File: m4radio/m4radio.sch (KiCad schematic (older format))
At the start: 36 parts, among them IC1 MCP2562, IC2 STM32F405RxTx, J1 WEST TOP, J2 EAST TOP, P1 SWD_TC, Y1 26M

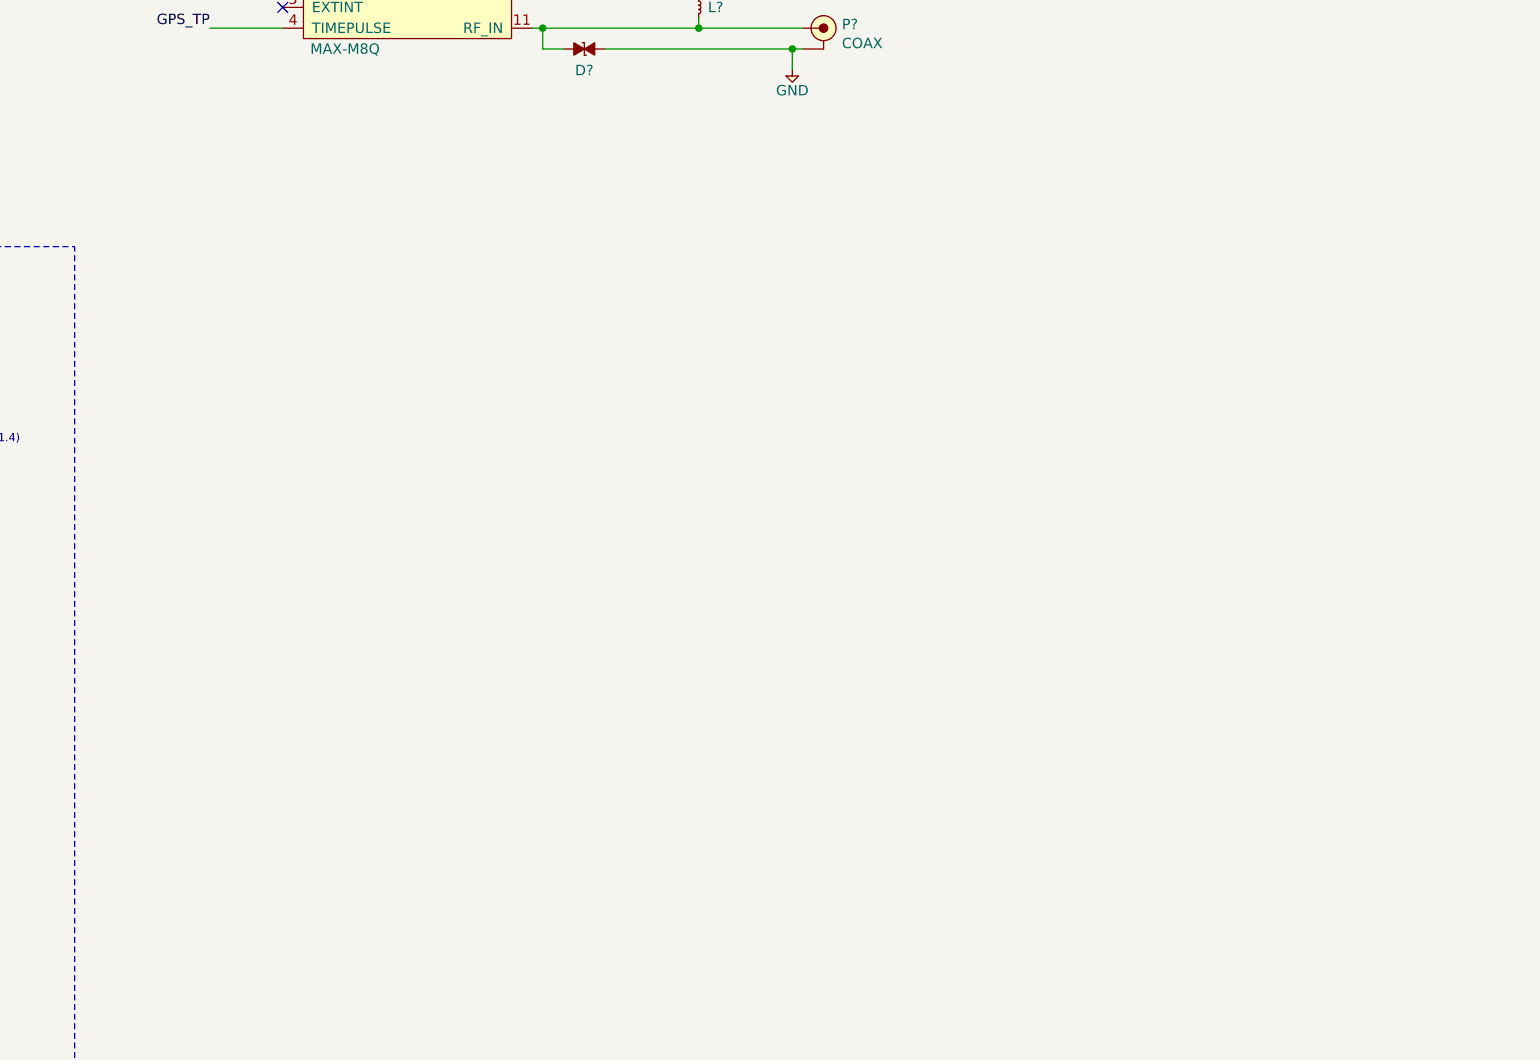
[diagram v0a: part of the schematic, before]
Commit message: Add PLL and radio ICs to schematic
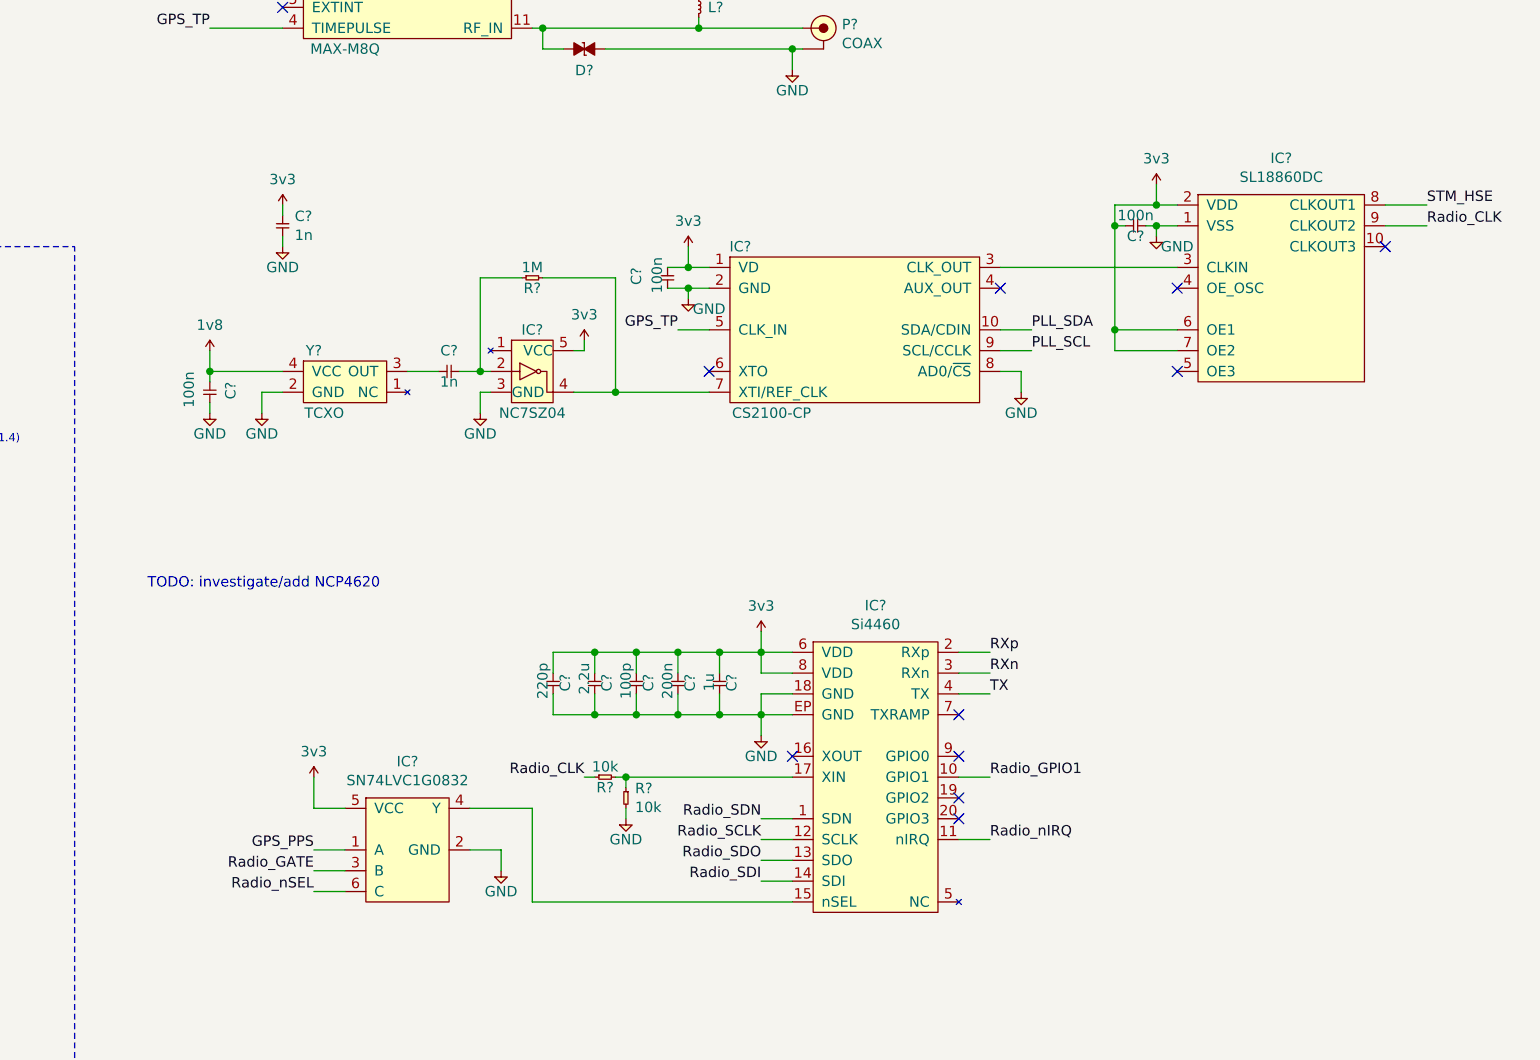
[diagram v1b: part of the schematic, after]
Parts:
- added C? (x3): 100n, symbol agg-kicad:C
- added C? (x2): 1n, symbol agg-kicad:C
- added C?: 1u, symbol agg-kicad:C
- added C?: 200n, symbol agg-kicad:C
- added C?: 100p, symbol agg-kicad:C
- added C?: 2.2u, symbol agg-kicad:C
- added C?: 220p, symbol agg-kicad:C
- added IC?: NC7SZ04, agg:SOT-23-5, symbol agg-kicad:NC7SZ04
- added IC?: CS2100-CP, agg:MSOP-10, symbol agg-kicad:CS2100-CP
- added IC?: SL18860DC, agg:DFN-10-SL18860DC, symbol agg-kicad:SL18860DC
- added IC?: SN74LVC1G0832, agg:SC-70-6, symbol agg-kicad:SN74LVC1G0832
- added IC?: Si4460, agg:QFN-20-EP-SI, symbol agg-kicad:Si4460
- added R?: 1M, symbol agg-kicad:R
- added R? (x2): 10k, symbol agg-kicad:R
- added Y?: TCXO, symbol agg-kicad:TCXO
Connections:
- net 3v3: now also C?.1, C?.1, C?.1, C?.1, C?.1, C?.1, C?.1, C?.2, IC?.1 (VD), IC?.2 (VDD), IC?.5 (VCC), IC?.5 (VCC), IC?.6 (OE1), IC?.6 (VDD), IC?.7 (OE2), IC?.8 (VDD)
- net GND: now also C?.1, C?.2, C?.2, C?.2, C?.2, C?.2, C?.2, C?.2, C?.2, IC?.1 (VSS), IC?.18 (GND), IC?.2 (GND), IC?.2 (GND), IC?.3 (GND), IC?.8 (AD0/~CS), IC?.EP (GND), R?.2, Y?.2 (GND)
- net GPS_PPS: now also IC?.1 (A)
- net GPS_TP: now also IC?.5 (CLK_IN)
- new net: C?.1, Y?.3 (OUT)
- new net: C?.2, IC?.2, R?.1
- new net: IC?.4, IC?.7 (XTI/REF_CLK), R?.2
- new net: IC?.3 (CLKIN), IC?.3 (CLK_OUT)
- new net: IC?.15 (nSEL), IC?.4 (Y)
- new net: IC?.17 (XIN), R?.1, R?.2
- new net 1v8: C?.1, Y?.4 (VCC)
- new net PLL_SCL: IC?.9 (SCL/CCLK)
- new net PLL_SDA: IC?.10 (SDA/CDIN)
- new net RXn: IC?.3 (RXn)
- new net RXp: IC?.2 (RXp)
- new net Radio_CLK: IC?.9 (CLKOUT2), R?.1
- new net Radio_GATE: IC?.3 (B)
- new net Radio_GPIO1: IC?.10 (GPIO1)
- new net Radio_SCLK: IC?.12 (SCLK)
- new net Radio_SDI: IC?.14 (SDI)
- new net Radio_SDN: IC?.1 (SDN)
- new net Radio_SDO: IC?.13 (SDO)
- new net Radio_nIRQ: IC?.11 (nIRQ)
- new net Radio_nSEL: IC?.6 (C)
- new net STM_HSE: IC?.8 (CLKOUT1)
- new net TX: IC?.4 (TX)
- no-connect marks 29 -> 39
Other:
- note added: "TODO: investigate/add NCP4620"

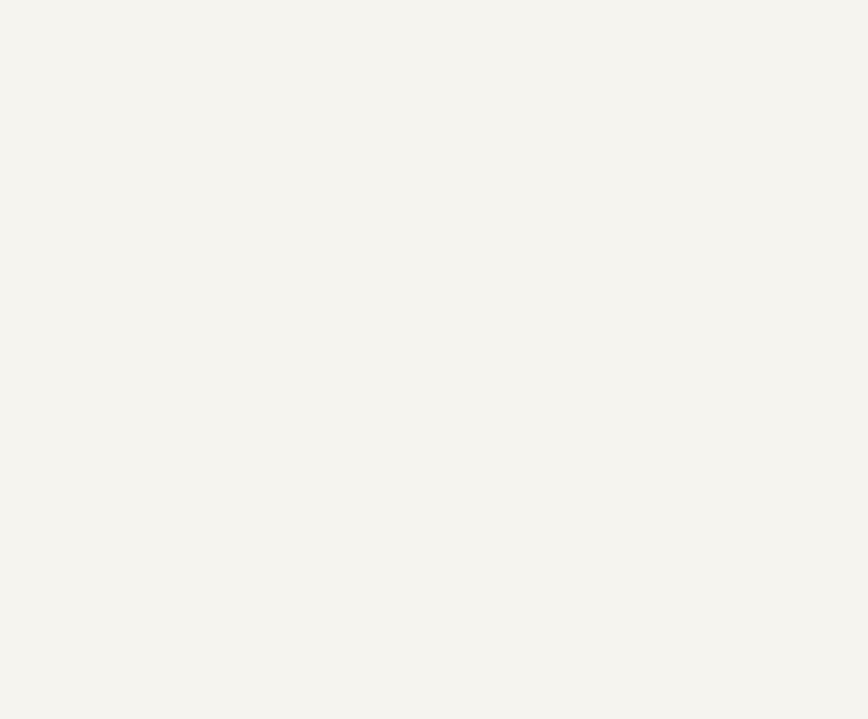
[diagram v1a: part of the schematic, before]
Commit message: Add filter/antenna connector
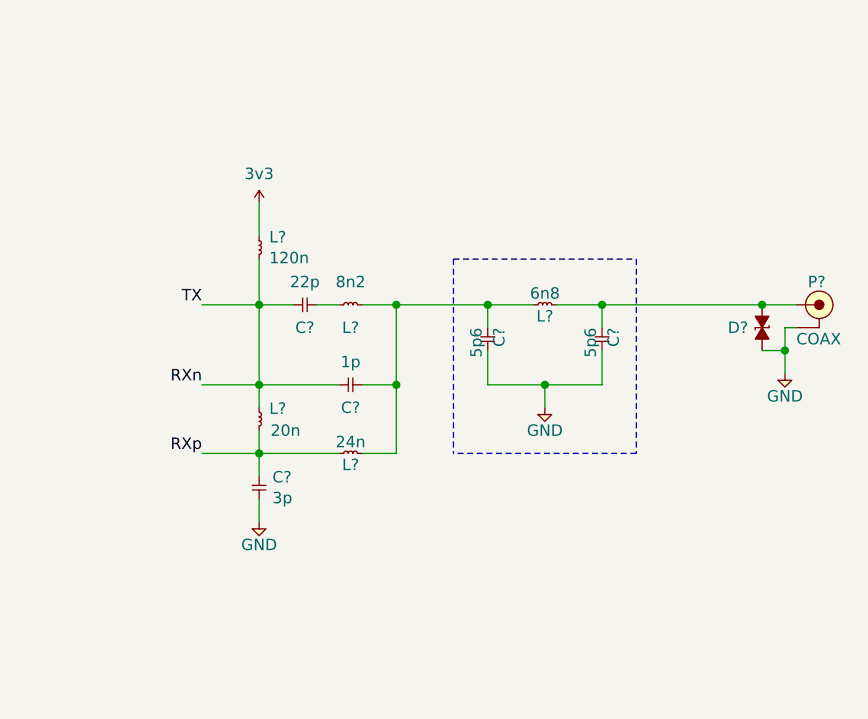
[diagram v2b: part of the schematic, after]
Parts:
- added C?: 3p, symbol agg-kicad:C
- added C?: 1p, symbol agg-kicad:C
- added C?: 22p, symbol agg-kicad:C
- added C? (x2): 5p6, symbol agg-kicad:C
- added D?: ESD_DIODE, agg:0402, symbol agg-kicad:ESD_DIODE
- added L?: 20n, symbol agg-kicad:L
- added L?: 24n, symbol agg-kicad:L
- added L?: 8n2, symbol agg-kicad:L
- added L?: 120n, symbol agg-kicad:L
- added L?: 6n8, symbol agg-kicad:L
- added P?: COAX, agg:SMA-EDGE, symbol agg-kicad:COAX
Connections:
- net TX is gone; now on net RXn: IC?.4 (TX)
- net 3v3: now also L?.1
- net GND: now also C?.2, C?.2, C?.2, D?.2, P?.2 (GND)
- net RXn: now also C?.1, C?.1, L?.1, L?.2
- net RXp: now also C?.1, L?.1, L?.2
- new net: C?.1, C?.2, L?.1, L?.2, L?.2
- new net: C?.2, L?.1
- new net: C?.1, D?.1, L?.2, P?.1 (RF)

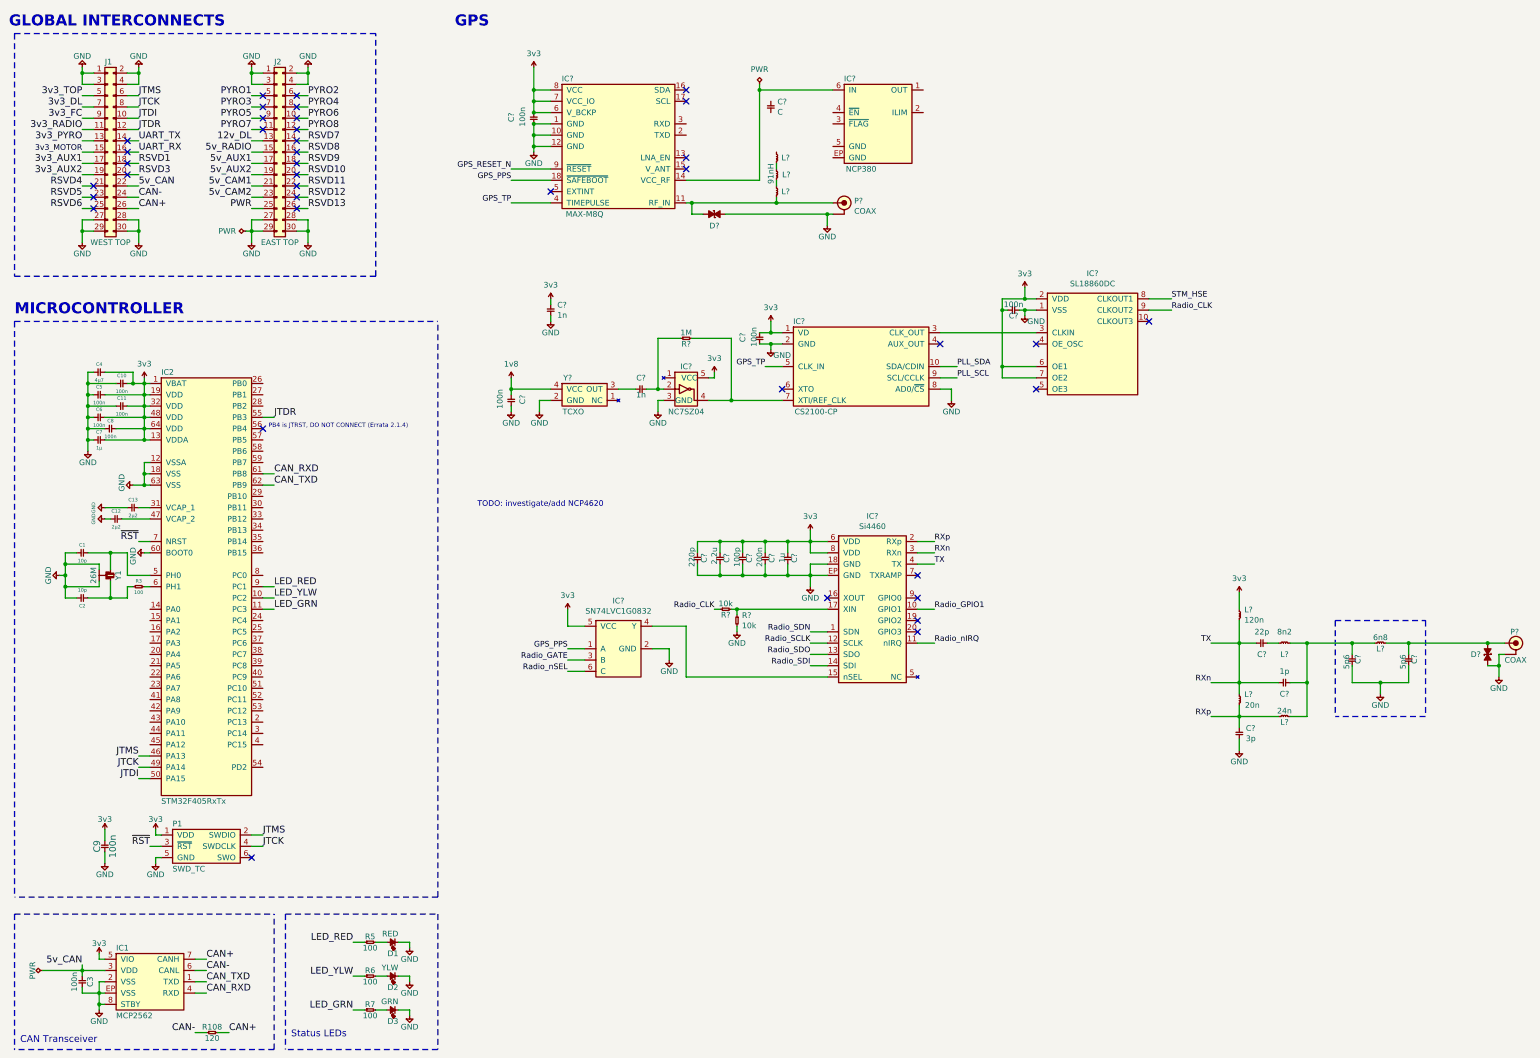
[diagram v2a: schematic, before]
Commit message: Finish GPS connections
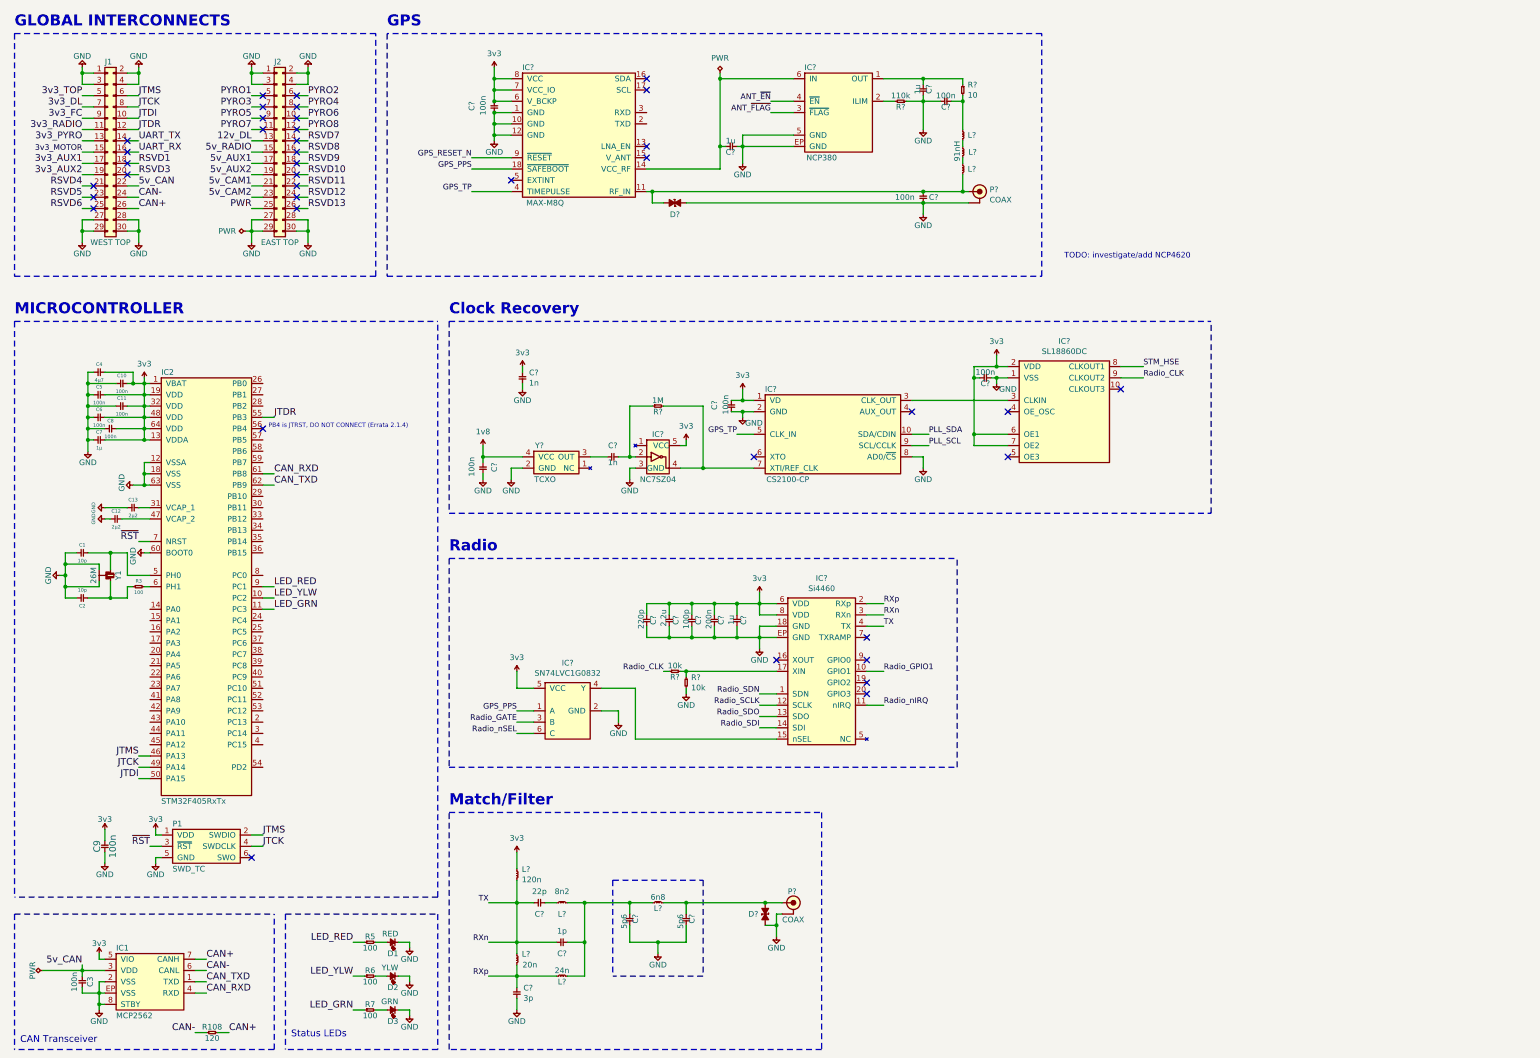
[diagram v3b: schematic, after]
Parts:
- added C? (x2): 100n, symbol agg-kicad:C
- added C?: 1u, symbol agg-kicad:C
- added R?: 110k, symbol agg-kicad:R
- added R?: 10, symbol agg-kicad:R
- C?: value C -> 1u
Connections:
- net GND: now also C?.2, IC?.5 (GND), IC?.EP (GND), C?.1, C?.1, C?.2, R?.1
- net at D?.1, IC?.11 (RF_IN), L?.2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: now also C?.1
- net at IC?.14 (VCC_RF), IC?.6 (IN): now also C?.1
- net at IC?.1 (OUT): now also C?.2, R?.1
- net at IC?.2 (ILIM): now also R?.2
- net ANT_~FLAG: now reaches IC?.3 (~FLAG)
- net ANT_~EN: now reaches IC?.4 (~EN)
- net at L?.1: now also C?.2, R?.2
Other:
- note added: "Clock Recovery"
- note added: "Match/Filter"
- note added: "Radio"
- moved on the sheet: C?, D?, IC?, L?, P?, R?, Y?

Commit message: Use caps for titles
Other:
- note added: "CLOCK RECOVERY"
- note added: "MATCH/FILTER"
- note added: "RADIO"
- note removed: "Clock Recovery"
- note removed: "Match/Filter"
- note removed: "Radio"
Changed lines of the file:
@@
 	4500 3350 11250 3350
 Text Notes 4500 3300 0    98   ~ 20
-Clock Recovery
+CLOCK RECOVERY
 Wire Notes Line
 	4500 5450 4500 7300
@@
 	11250 5050 11250 3350
 Text Notes 4500 5400 0    98   ~ 20
-Radio
+RADIO
 Wire Notes Line
 	4500 7700 7800 7700
 Text Notes 4500 7650 0    98   ~ 20
-Match/Filter
+MATCH/FILTER
 Wire Notes Line
 	7800 7700 7800 9800
